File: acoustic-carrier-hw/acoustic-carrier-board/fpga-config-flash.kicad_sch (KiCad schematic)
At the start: 24 parts, among them IC1 ECP5-BGA256, J701 Conn_02x03_Odd_Even, J702 PMOD_JTAG, J703 PMOD_SPI, SW701 SW_Push, U701 W25Q128JVS, U702 W25Q128JVS

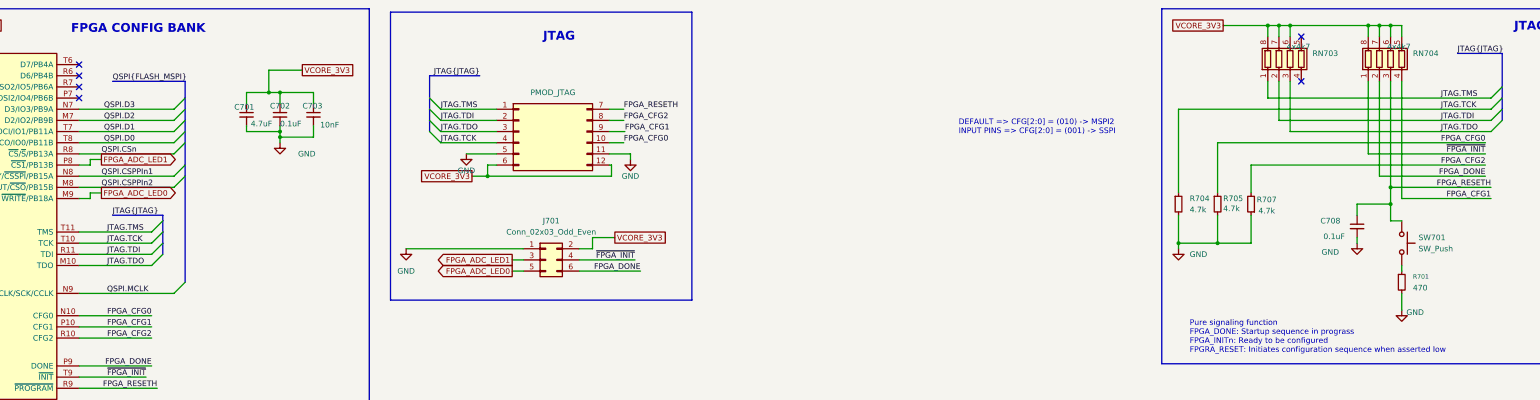
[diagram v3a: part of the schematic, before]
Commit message: [carrier] finished final review, (next) posting to linkedin, start working on analog front-end board
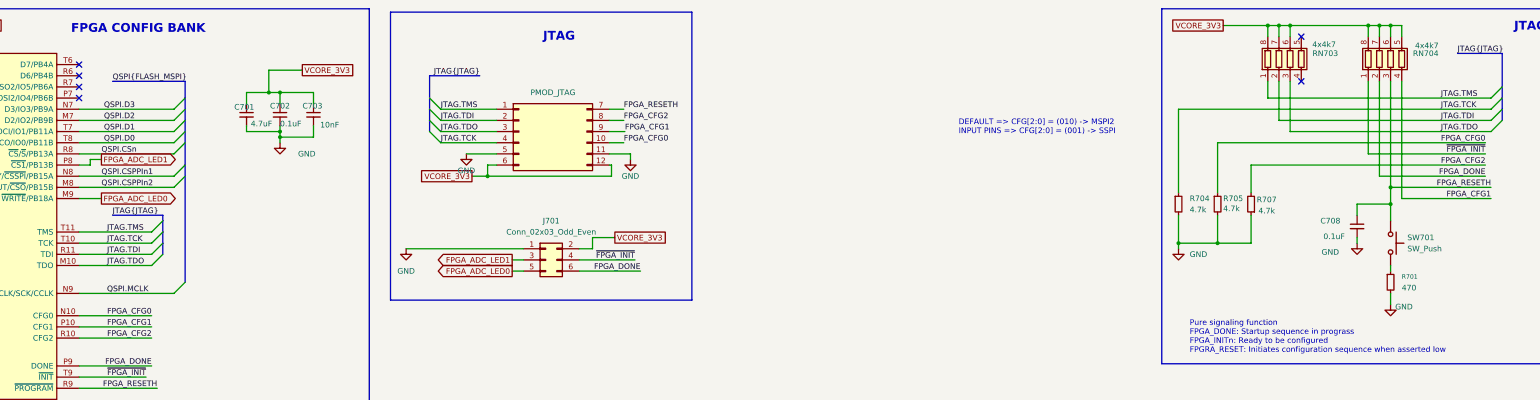
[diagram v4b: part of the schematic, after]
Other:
- moved on the sheet: R701, SW701
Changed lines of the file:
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@@
 	(wire
 		(pts
-			(xy 63.5 59.69) (xy 60.96 59.69)
+			(xy 60.96 59.69) (xy 66.04 59.69)
 		)
 		(stroke
@@
 	(wire
 		(pts
-			(xy 66.04 58.42) (xy 63.5 58.42)
-		)
-		(stroke
-			(width 0)
-			(type default)
-		)
-	)
-	(wire
-		(pts
 			(xy 185.166 44.45) (xy 181.61 44.45)
 		)
@@
 	(wire
 		(pts
-			(xy 361.95 74.93) (xy 361.95 76.2)
+			(xy 359.41 74.93) (xy 359.41 76.2)
 		)
 		(stroke
@@
 	(wire
 		(pts
-			(xy 361.95 81.28) (xy 361.95 85.09)
+			(xy 359.41 81.28) (xy 359.41 83.82)
 		)
 		(stroke
@@
 	(wire
 		(pts
-			(xy 359.41 64.77) (xy 361.95 64.77)
-		)
-		(stroke
-			(width 0)
-			(type default)
-		)
-	)
-	(wire
-		(pts
 			(xy 320.04 69.85) (xy 327.66 69.85)
 		)
@@
 	(wire
 		(pts
-			(xy 63.5 58.42) (xy 63.5 59.69)
-		)
-		(stroke
-			(width 0)
-			(type default)
-		)
-	)
-	(wire
-		(pts
 			(xy 255.27 132.08) (xy 255.27 142.24)
 		)
@@
 	(global_label "FPGA_ADC_LED0"
 		(shape output)
-		(at 66.04 58.42 0)
+		(at 66.04 59.69 0)
 		(fields_autoplaced yes)
 		(effects
@@
 		)
 		(property "Intersheetrefs" "${INTERSHEET_REFS}"
-			(at 83.9628 58.42 0)
+			(at 83.9628 59.69 0)
 			(effects
 				(font
@@
 		)
 		(property "Value" "4x4k7"
-			(at 341.122 25.146 0)
+			(at 346.964 24.638 0)
 			(effects
 				(font
@@
 	(symbol
 		(lib_id "power:GND")
-		(at 361.95 85.09 0)
+		(at 359.41 83.82 0)
 		(unit 1)
 		(exclude_from_sim no)
@@
 		(dnp no)
 		(property "Reference" "#PWR0702"
-			(at 361.95 91.44 0)
+			(at 359.41 90.17 0)
 			(effects
 				(font
@@
 		)
 		(property "Value" "GND"
-			(at 364.998 85.598 0)
+			(at 362.458 84.328 0)
 			(effects
 				(font
@@
 		)
 		(property "Footprint" ""
-			(at 361.95 85.09 0)
+			(at 359.41 83.82 0)
 			(effects
 				(font
@@
 		)
 		(property "Datasheet" ""
-			(at 361.95 85.09 0)
+			(at 359.41 83.82 0)
 			(effects
 				(font
@@
 		)
 		(property "Description" "Power symbol creates a global label with name \"GND\" , ground"
-			(at 361.95 85.09 0)
+			(at 359.41 83.82 0)
 			(effects
 				(font
@@
 	(symbol
 		(lib_id "Device:R_Small")
-		(at 361.95 78.74 0)
+		(at 359.41 78.74 0)
 		(unit 1)
 		(exclude_from_sim no)
@@
 		(fields_autoplaced yes)
 		(property "Reference" "R701"
-			(at 364.49 77.4699 0)
+			(at 361.95 77.4699 0)
 			(effects
 				(font
@@
 		)
 		(property "Value" "470"
-			(at 364.49 80.0099 0)
+			(at 361.95 80.0099 0)
 			(effects
 				(font
@@
 		)
 		(property "Footprint" "Resistor_SMD:R_0402_1005Metric"
-			(at 361.95 78.74 0)
+			(at 359.41 78.74 0)
 			(effects
 				(font
@@
 		)
 		(property "Datasheet" "https://jlcpcb.com/api/file/downloadByFileSystemAccessId/8579705913233424384"
-			(at 361.95 78.74 0)
+			(at 359.41 78.74 0)
 			(effects
 				(font
@@
 		)
 		(property "Description" "Resistor, small symbol"
-			(at 361.95 78.74 0)
+			(at 359.41 78.74 0)
 			(effects
 				(font
@@
 		)
 		(property "MPN" "0402WGF4700TCE"
-			(at 361.95 78.74 0)
+			(at 359.41 78.74 0)
 			(effects
 				(font
@@
 		)
 		(property "LPN" "C25117"
-			(at 361.95 78.74 0)
+			(at 359.41 78.74 0)
 			(effects
 				(font
@@
 	(symbol
 		(lib_id "Switch:SW_Push")
-		(at 361.95 69.85 270)
+		(at 359.41 69.85 270)
 		(unit 1)
 		(exclude_from_sim no)
@@
 		(fields_autoplaced yes)
 		(property "Reference" "SW701"
-			(at 365.76 68.5799 90)
+			(at 363.22 68.5799 90)
 			(effects
 				(font
@@
 		)
 		(property "Value" "SW_Push"
-			(at 365.76 71.1199 90)
+			(at 363.22 71.1199 90)
 			(effects
 				(font
@@
 		)
 		(property "Footprint" "iw-misc:SW_TS-1088-AR02016"
-			(at 367.03 69.85 0)
+			(at 364.49 69.85 0)
 			(effects
 				(font
@@
 		)
 		(property "Datasheet" "https://jlcpcb.com/api/file/downloadByFileSystemAccessId/8588886944068096000"
-			(at 367.03 69.85 0)
+			(at 364.49 69.85 0)
 			(effects
 				(font
@@
 		)
 		(property "Description" "Push button switch, generic, two pins"
-			(at 361.95 69.85 0)
+			(at 359.41 69.85 0)
 			(effects
 				(font
@@
 		)
 		(property "LPN" "C720477"
-			(at 361.95 69.85 90)
+			(at 359.41 69.85 90)
 			(effects
 				(font
@@
 		)
 		(property "MPN" "TS-1088-AR02016"
-			(at 361.95 69.85 90)
+			(at 359.41 69.85 90)
 			(effects
 				(font
@@
 		)
 		(property "Value" "4x4k7"
-			(at 363.982 25.146 0)
+			(at 370.332 24.892 0)
 			(effects
 				(font

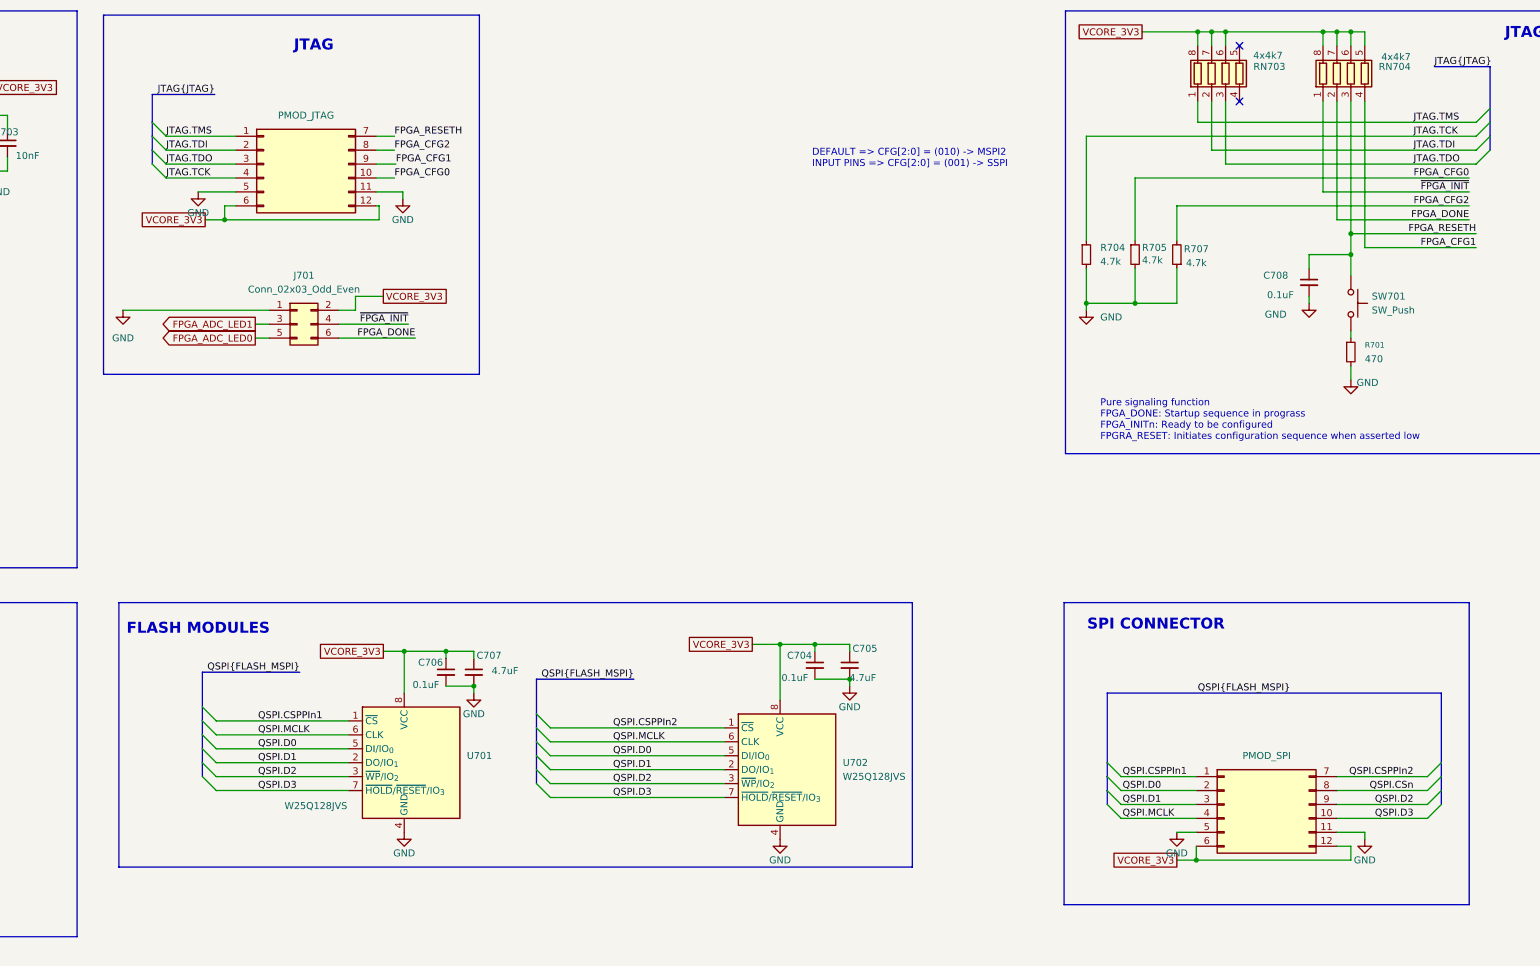
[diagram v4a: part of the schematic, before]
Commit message: [carrier] finished for production (next) reroute the LPDDR3, with appropriate CMD-CTRL bus delays, and change banks for command-control
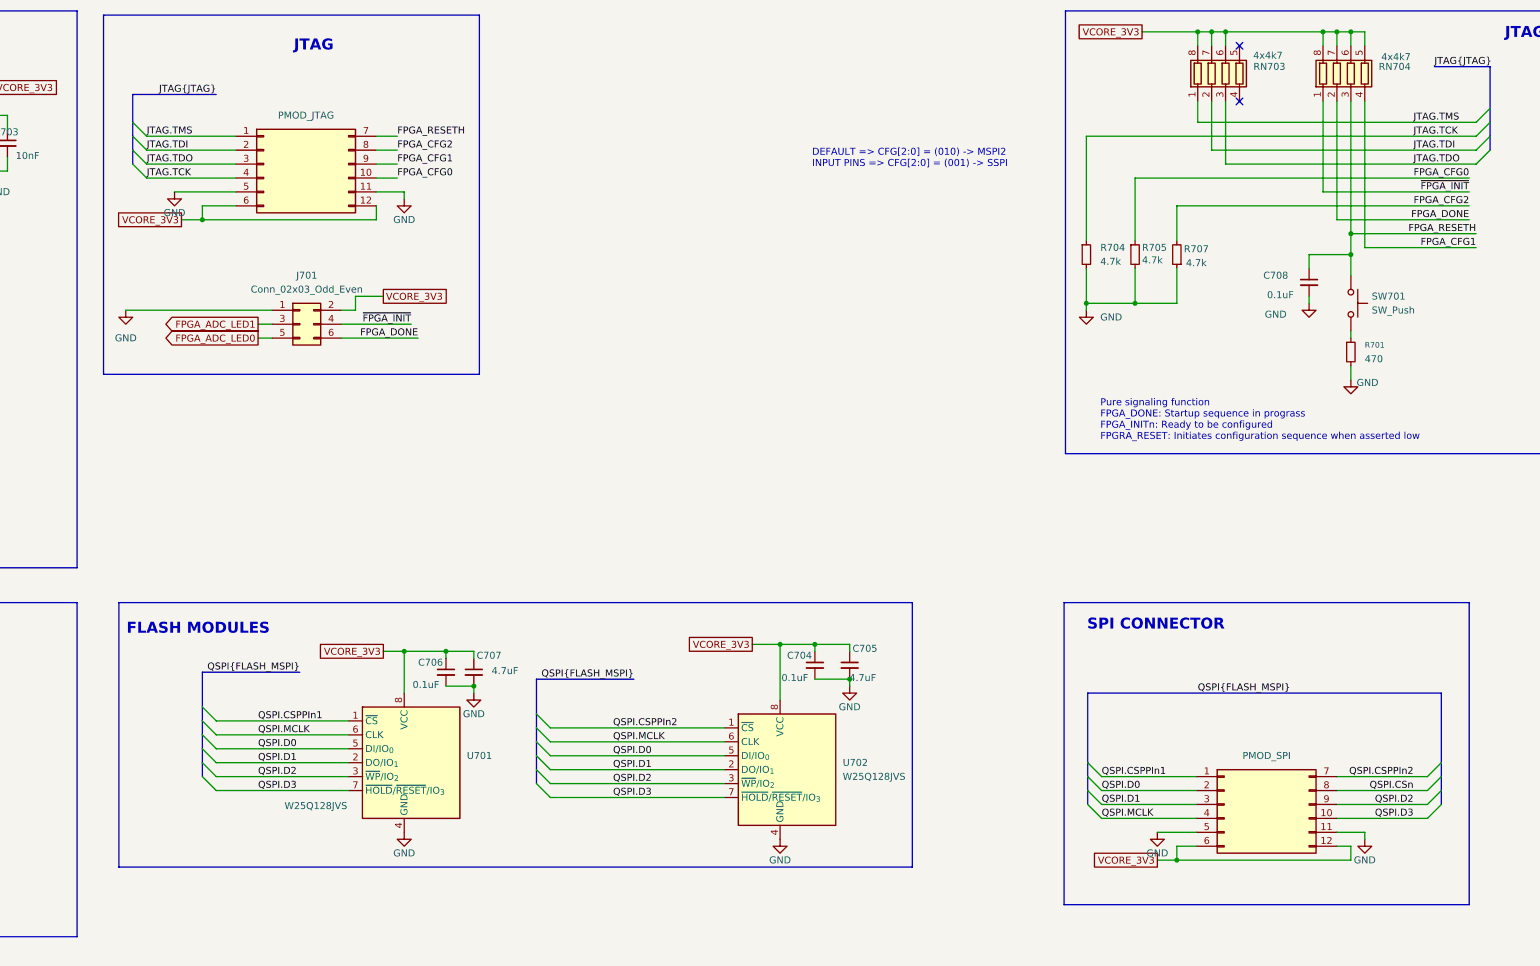
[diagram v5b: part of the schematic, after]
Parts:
- IC1: Manufacturer Lattice -> (none)
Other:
- moved on the sheet: J701
